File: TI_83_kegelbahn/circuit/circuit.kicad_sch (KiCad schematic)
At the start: 12 parts, among them K1 ATmega328P-P, SW1 SW_DPST_x2, X1 DE9_Pins, X2 DE9_Pins, Y1 16M

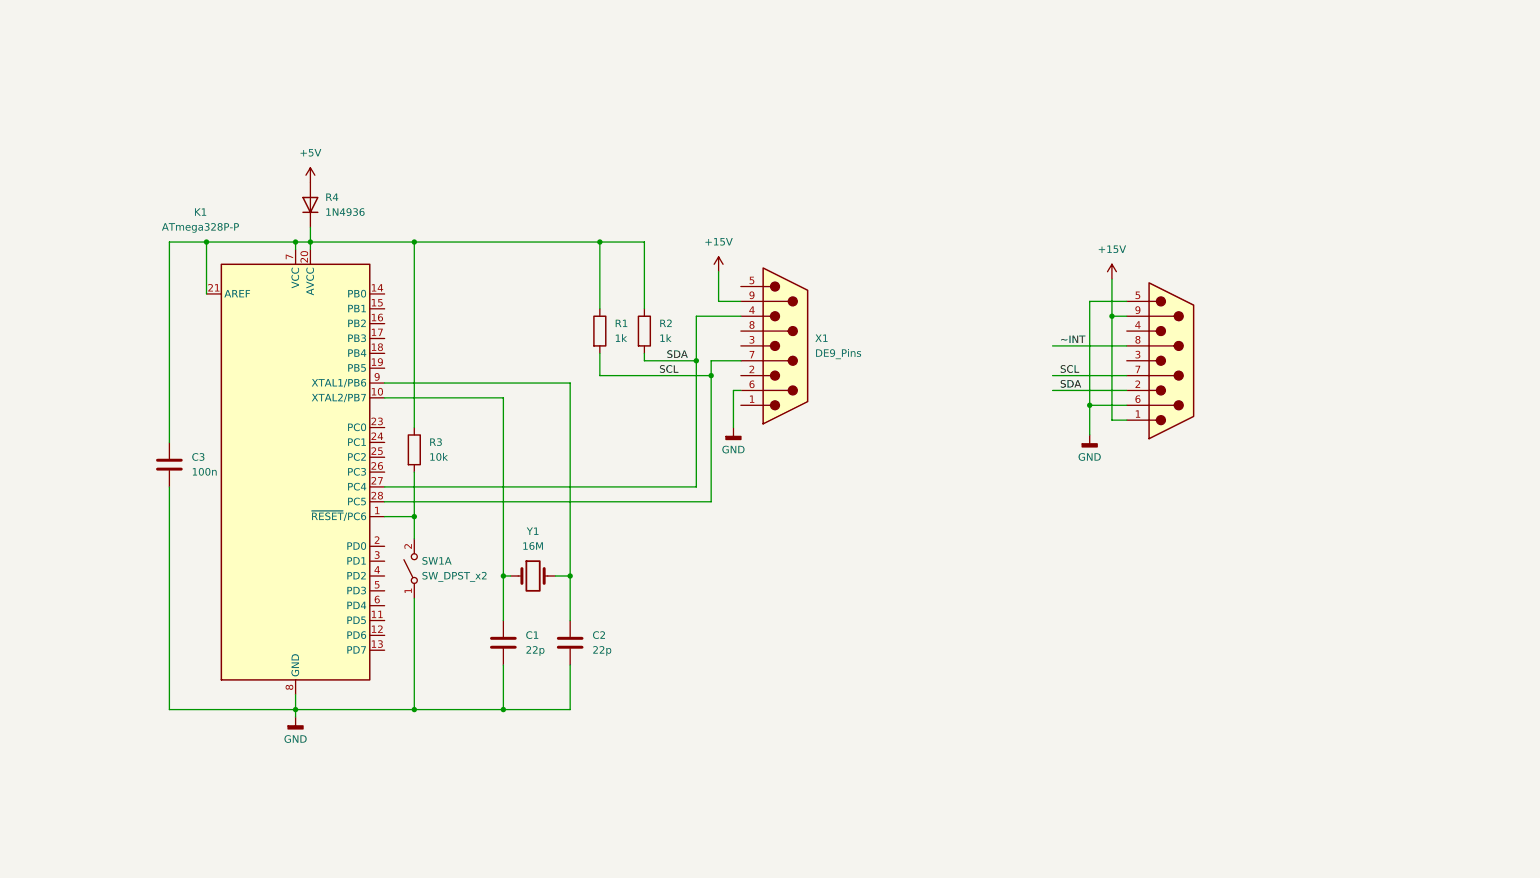
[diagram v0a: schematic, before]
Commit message: docs(kegelbahn): Kegelbahnanzeige mit AT90CAN32
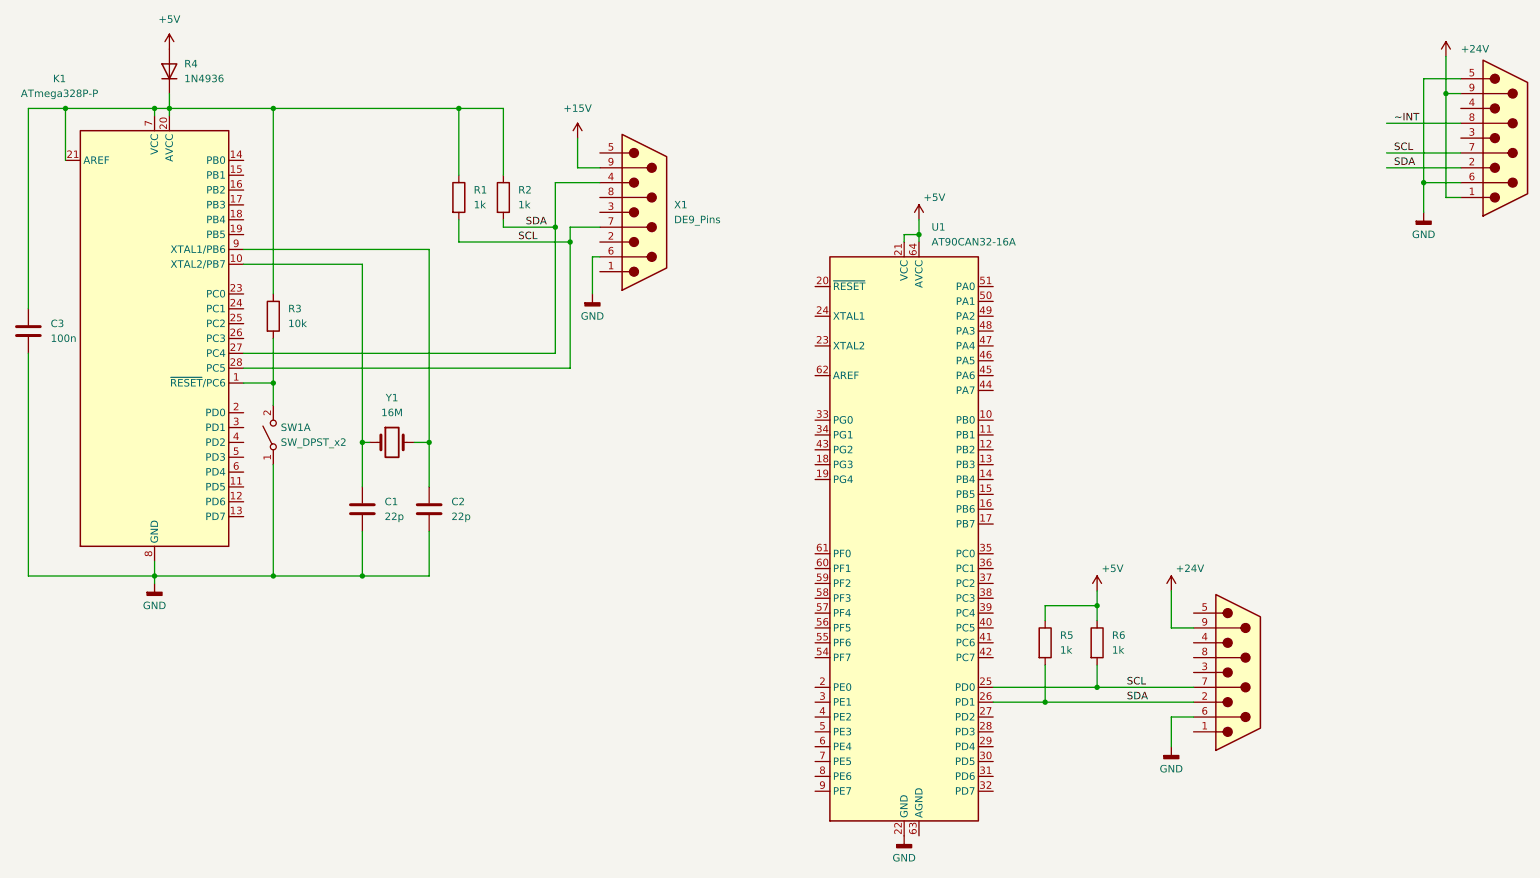
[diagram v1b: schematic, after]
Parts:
- added R5, R6: 1k, symbol Device:R
- added U1: AT90CAN32-16A, Package_QFP:TQFP-64_14x14mm_P0.8mm, symbol MCU_Microchip_AVR:AT90CAN32-16A
- added X3: DE9_Pins, symbol Connector:DE9_Pins
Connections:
- net +15V: no longer X2.1, X2.9
- net +5V: now also R5.1, R6.1, U1.21 (VCC), U1.52 (VCC), U1.64 (AVCC)
- net GND: now also U1.22 (GND), U1.53 (GND), X3.6
- net SCL: now also R6.2, U1.25 (PD0), X3.7
- net SDA: now also R5.2, U1.26 (PD1), X3.2
- new net +24V: X2.1, X2.9, X3.9
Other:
- moved on the sheet: C1, C2, C3, K1, R1, R2, R3, R4, SW1A, X1, Y1
